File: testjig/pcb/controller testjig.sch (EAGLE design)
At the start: 50 parts, among them IC1 AD8041R, J1 POWER_JACKPTH, SW2 BUTTON_2

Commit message: Bringing up the test rig
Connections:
- net TARGET_001_MEAS renamed TARGET_VBAT_MEAS
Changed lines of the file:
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@@
 </segment>
 </net>
-<net name="TARGET_001_MEAS" class="0">
+<net name="TARGET_VBAT_MEAS" class="0">
 <segment>
 <pinref part="U$1" gate="G$1" pin="14/A0"/>

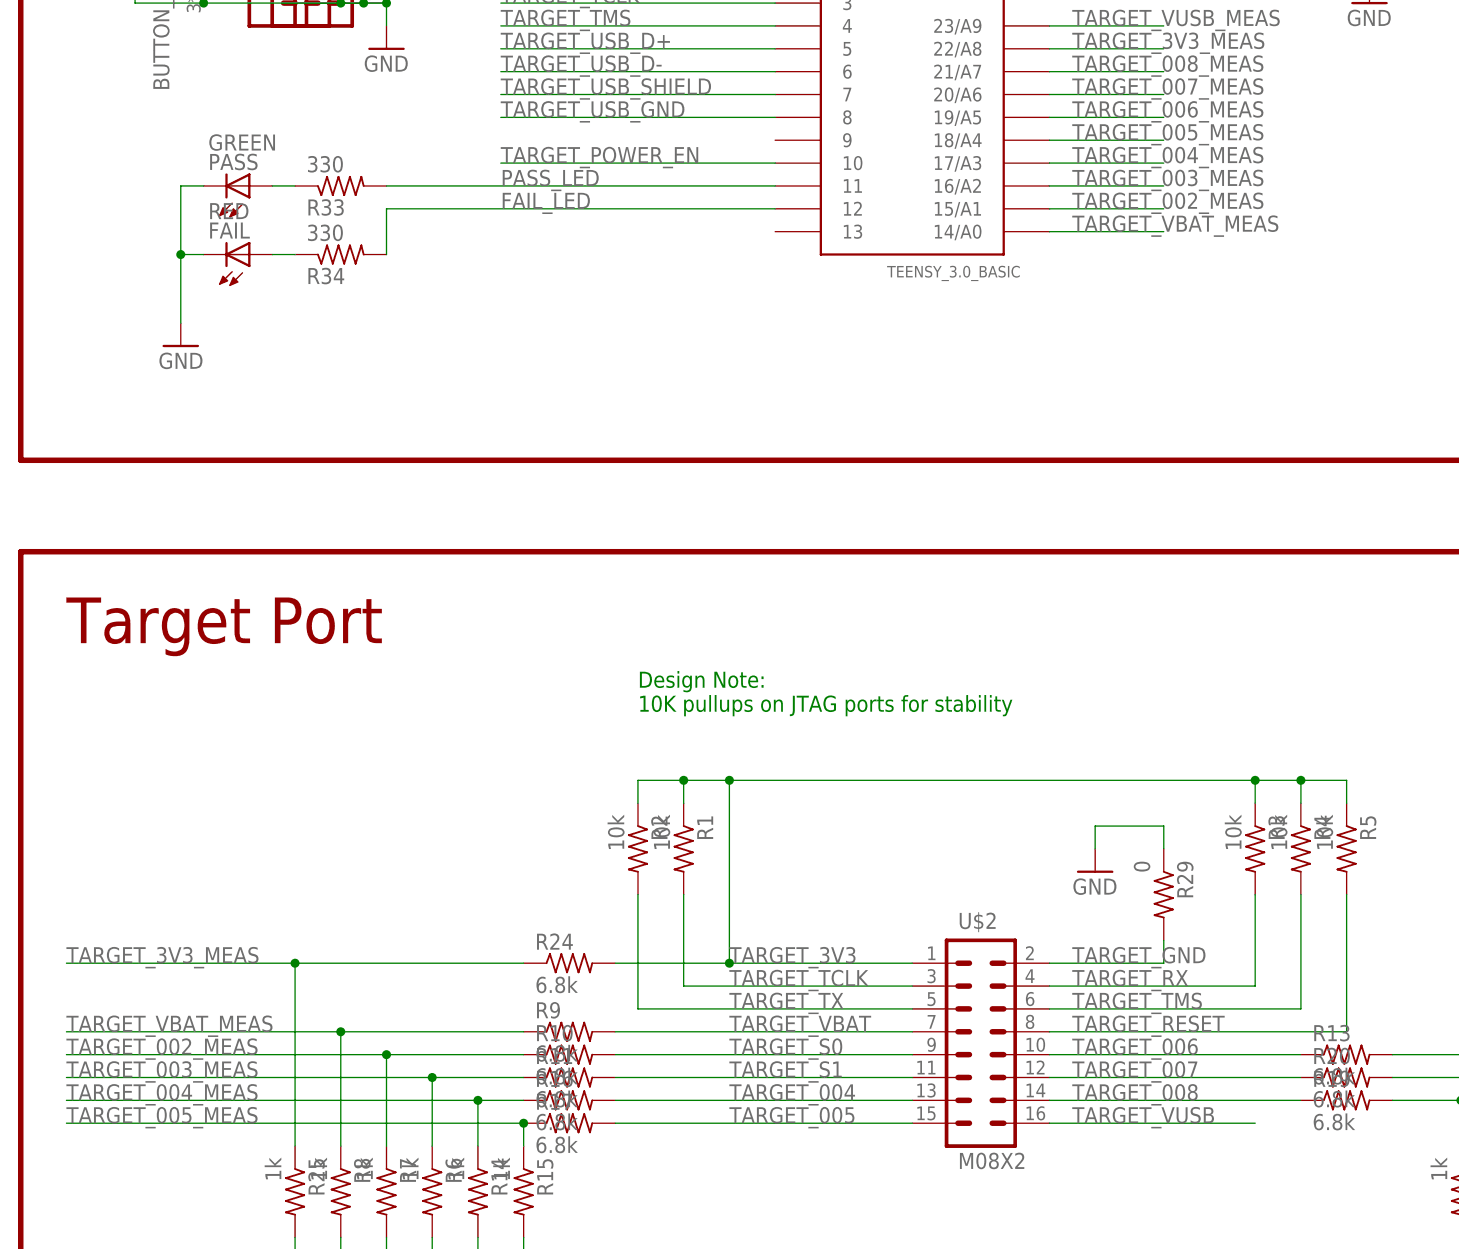
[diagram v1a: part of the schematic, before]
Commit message: Add S0, S1 tests, begin I2C work for accelerometer
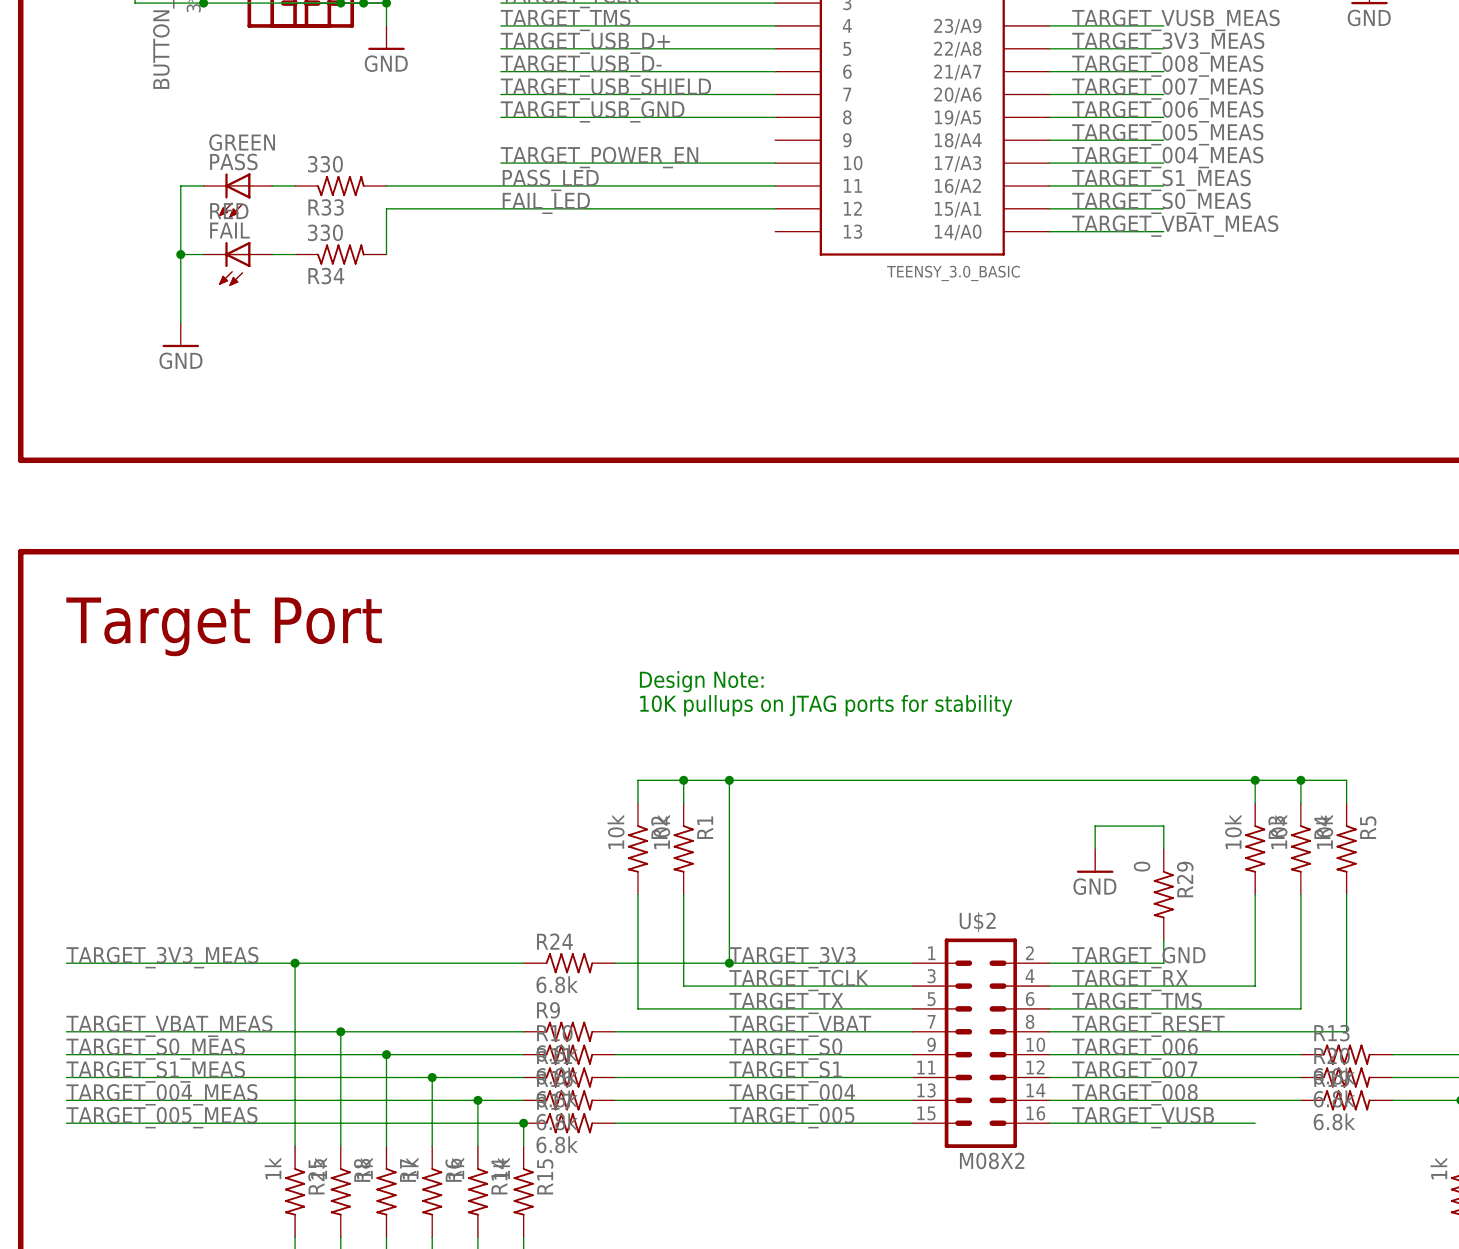
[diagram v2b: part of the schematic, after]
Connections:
- net TARGET_002_MEAS renamed TARGET_S0_MEAS
- net TARGET_003_MEAS renamed TARGET_S1_MEAS
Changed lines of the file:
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@@
 </segment>
 </net>
-<net name="TARGET_003_MEAS" class="0">
+<net name="TARGET_S1_MEAS" class="0">
 <segment>
 <pinref part="U$1" gate="G$1" pin="16/A2"/>
@@
 </segment>
 </net>
-<net name="TARGET_002_MEAS" class="0">
+<net name="TARGET_S0_MEAS" class="0">
 <segment>
 <pinref part="U$1" gate="G$1" pin="15/A1"/>

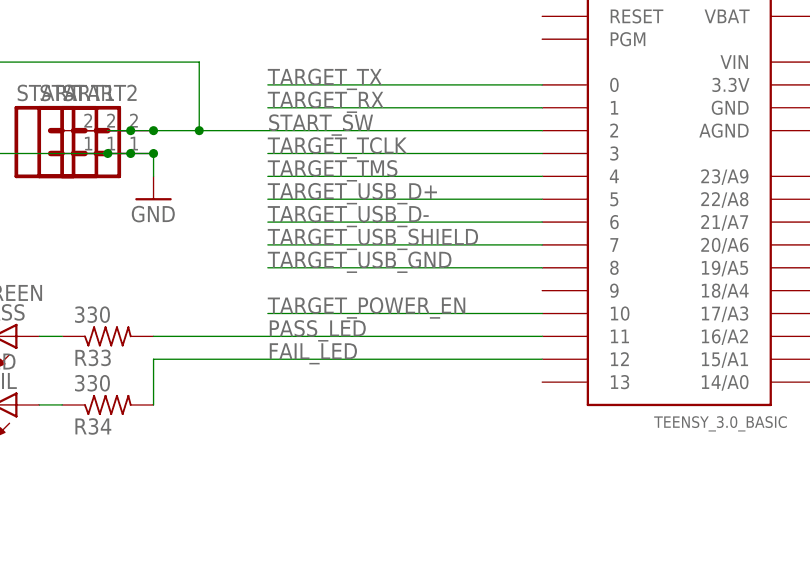
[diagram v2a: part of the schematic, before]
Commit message: Fix target poweroff routine, add nonworking LED test
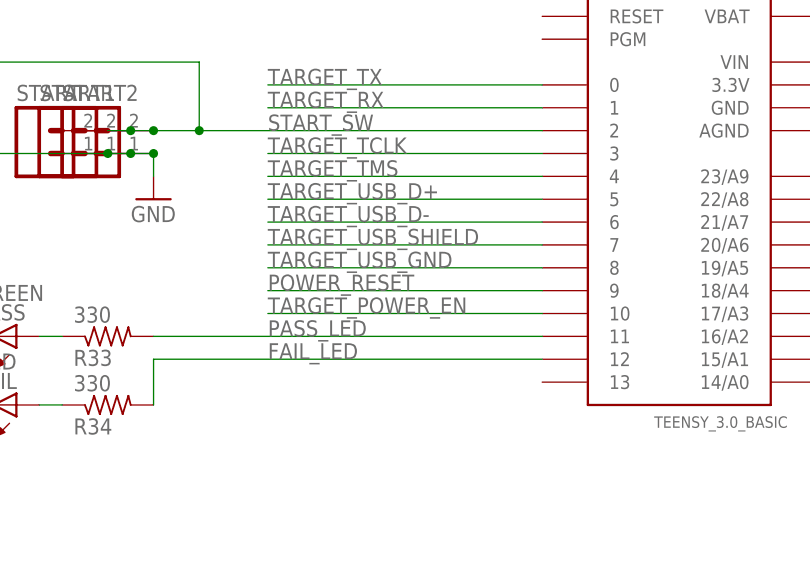
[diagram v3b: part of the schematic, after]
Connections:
- new net POWER_RESET: U$1.9
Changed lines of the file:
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@@
+</segment>
+</net>
+<net name="POWER_RESET" class="0">
+<segment>
+<pinref part="U$1" gate="G$1" pin="9"/>
+<wire x1="-48.26" y1="20.32" x2="-78.74" y2="20.32" width="0.1524" layer="91"/>
+<label x="-78.74" y="20.32" size="1.778" layer="95"/>
 </segment>
 </net>
